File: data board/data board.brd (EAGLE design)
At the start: 31.6 x 28 mm, 28 parts, among them IC1 93LC56B, IC2 FT232HQ, X6 USBC, Y1 12MHz

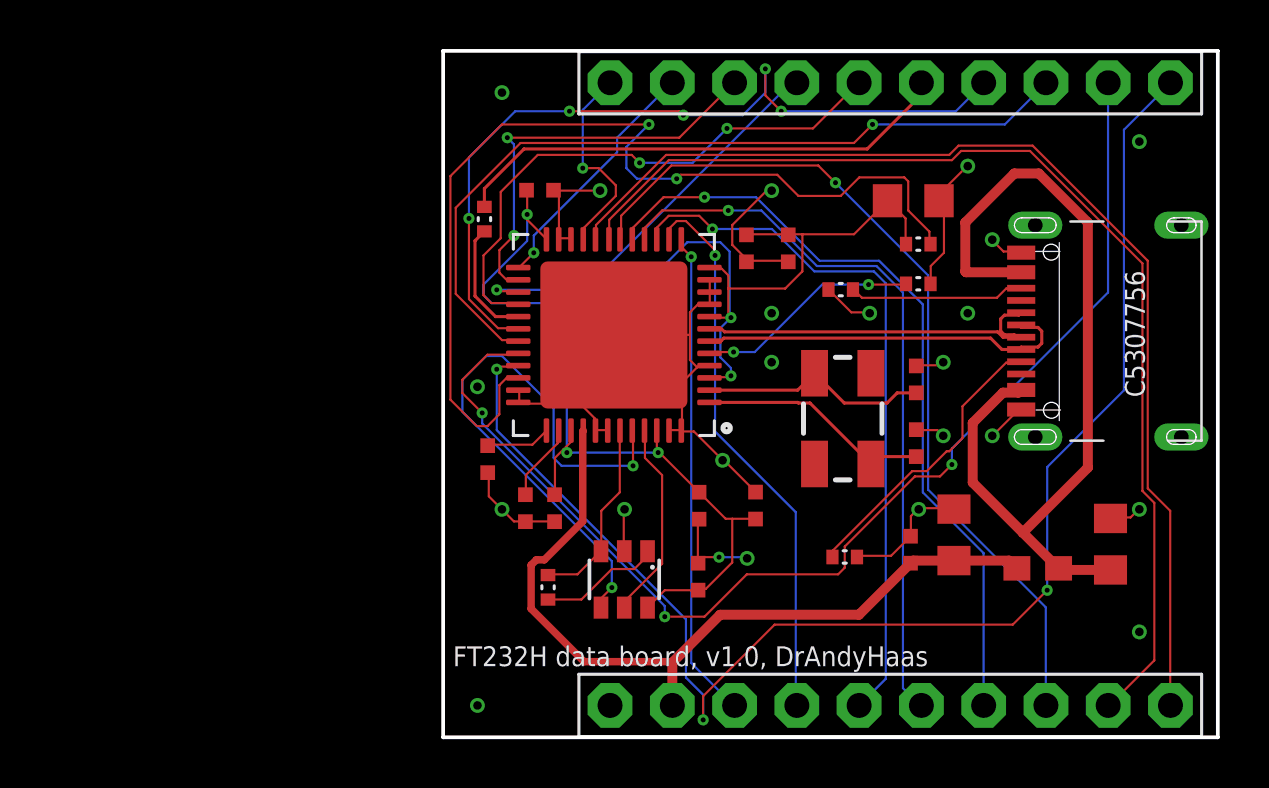
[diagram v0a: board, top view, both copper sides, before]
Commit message: add husb238 for power delivery
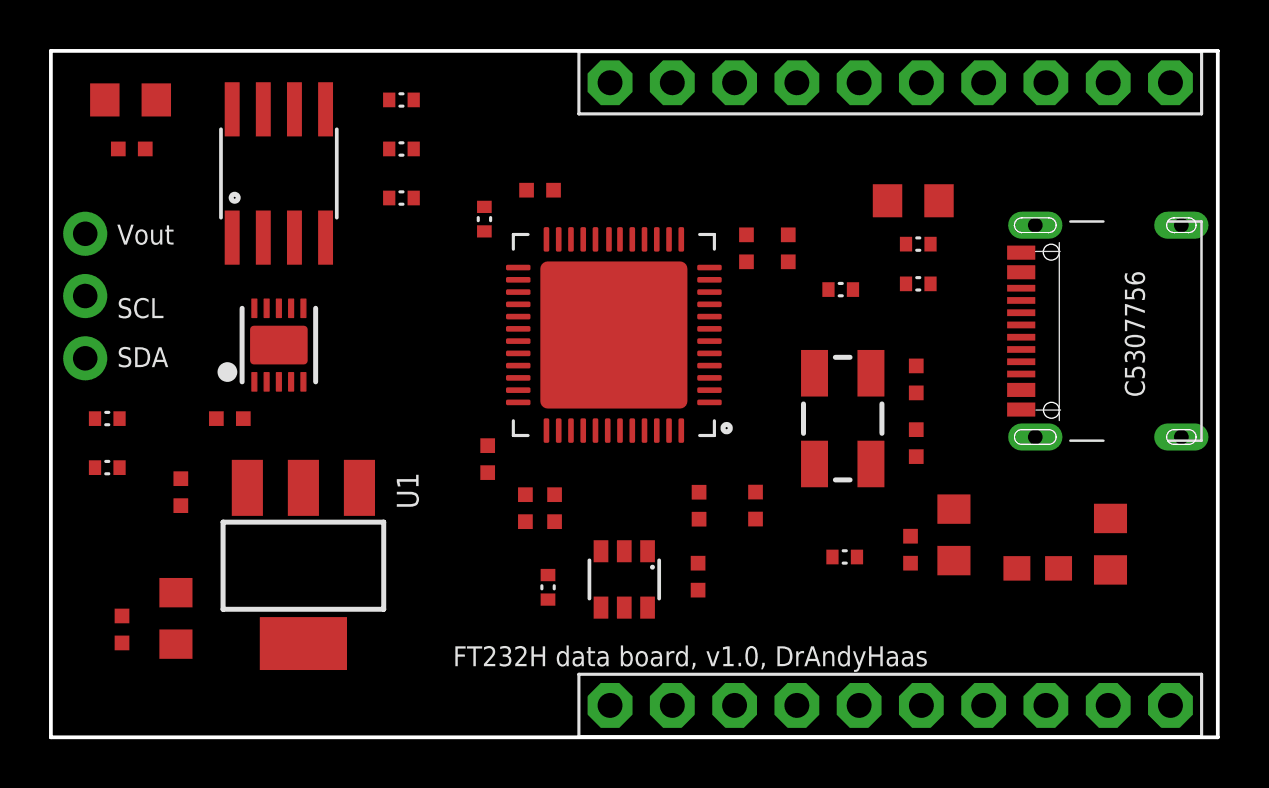
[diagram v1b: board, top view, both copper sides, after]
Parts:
- added C16: 1uF, Nordic_nRF:RESC0402_N
- added C17, C19: 10uF, Nordic_nRF:RESC0805_N
- added C18, C20, C21: 0.1uF, Nordic_nRF:RESC0402_N
- added JP3: (no value), microbuilder:1X03_ROUND
- added R10, R13: 10k, FlashPCB_Resistors:RES-0402
- added R7: 10, FlashPCB_Resistors:RES-0402
- added R8: 5.1k, FlashPCB_Resistors:RES-0402
- added R9: 49.9k, FlashPCB_Resistors:RES-0402
- added U$9: MOSFET-PCHANNEL-SOIC8SOIC8, SparkFun-DiscreteSemi:SO08
- added U1: CJT1117-5.0-SOT223, Seeed-IC:SOT-223
- added X3: HUSB238, adafruit_power:DFN10_3X3MM
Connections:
- new net GATE: R8.P$2, R9.P$1, U$9.4
- new net N$13: R13.P$1, X3.8
- new net N$14: R10.P$1, X3.9
- new net N$6: C16.2, R7.P$1, X3.1
- new net N$8: R8.P$1, X3.10
- new net SCL: JP3.2, X3.7
- new net SDA: JP3.3, X3.6
- new net VOUT: C17.2, C18.2, C21.2, JP3.1, U$9.5, U$9.6, U$9.7, U$9.8, U1.3
- net 5V: now also C19.2, C20.2, U1.2, U1.TER
- net CC1: now also X3.4
- net CC2: now also X3.5
- net D_N: now also X3.3
- net D_P: now also X3.2
- net GND: now also C16.1, C17.1, C18.1, C19.1, C20.1, C21.1, R10.P$2, R13.P$2, U1.1, X3.GND
- net VBUS: now also R7.P$2, R9.P$2, U$9.1, U$9.2, U$9.3
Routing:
- net VCC3V3: track 65.9 -> 0.00 mm, vias 5 -> 0
- net GND: track 63.8 -> 0.00 mm, vias 23 -> 0
- net C9: track 58.3 -> 0.00 mm, vias 3 -> 0
- net C8: track 48.8 -> 0.00 mm, vias 3 -> 0
- net D7: track 44.9 -> 0.00 mm
- net D6: track 44.7 -> 0.00 mm
- net N$7: track 40.4 -> 0.00 mm, vias 2 -> 0
- net VBUS: track 36.8 -> 0.00 mm
- net D5: track 35.7 -> 0.00 mm, vias 1 -> 0
- net C6: track 33.3 -> 0.00 mm, vias 5 -> 0
- net C7: track 33.1 -> 0.00 mm, vias 1 -> 0
- net 5V: track 32.6 -> 0.00 mm
- net D4: track 32.0 -> 0.00 mm, vias 1 -> 0
- net D3: track 29.9 -> 0.00 mm, vias 1 -> 0
- net D2: track 28.8 -> 0.00 mm, vias 1 -> 0
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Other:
- board size 31.6 x 28 mm -> 47.6 x 28 mm
- board text added: "SCL"
- board text added: "SDA"
- board text added: "Vout"

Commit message: Revert "add husb238 for power delivery"
This reverts commit fdcc09ca80390afb5c840c7f1bf23dbb25893304.
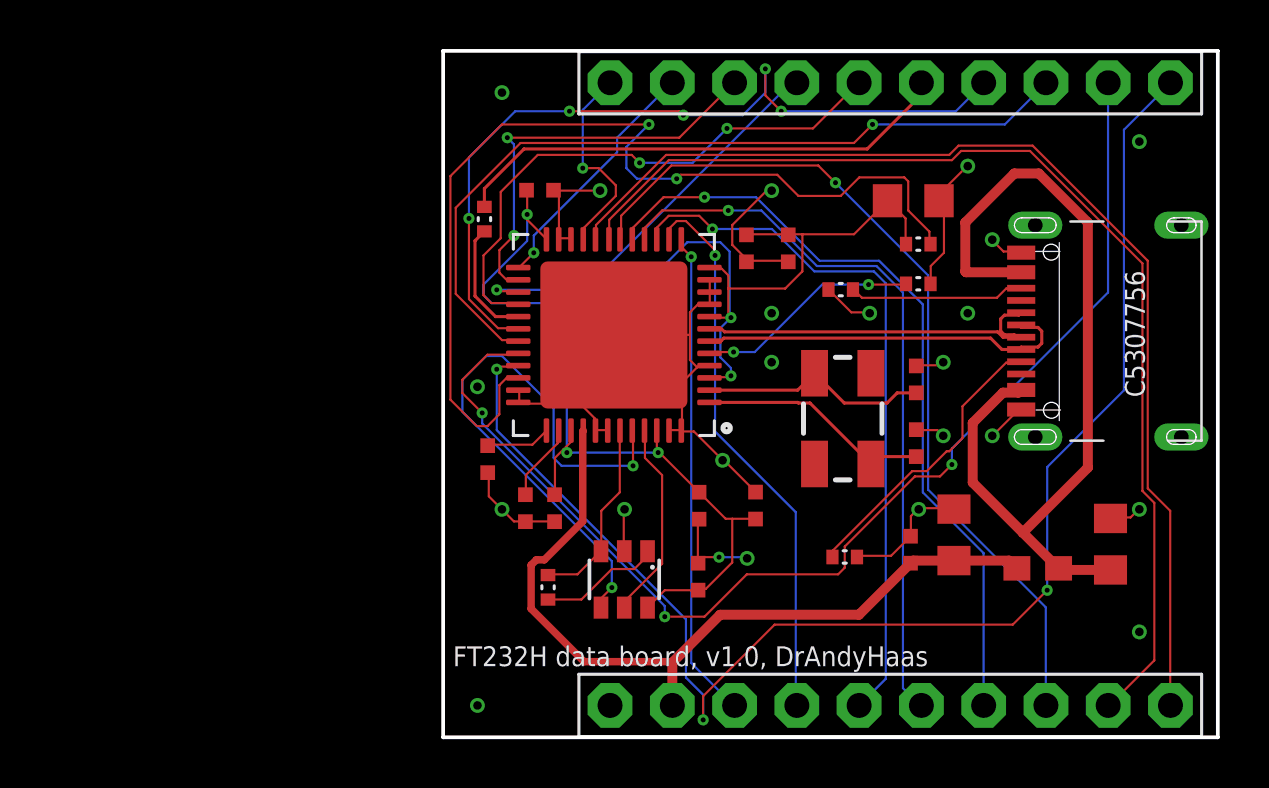
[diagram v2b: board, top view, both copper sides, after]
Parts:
- removed C16: 1uF, Nordic_nRF:RESC0402_N
- removed C17, C19: 10uF, Nordic_nRF:RESC0805_N
- removed C18, C20, C21: 0.1uF, Nordic_nRF:RESC0402_N
- removed JP3: (no value), microbuilder:1X03_ROUND
- removed R10, R13: 10k, FlashPCB_Resistors:RES-0402
- removed R7: 10, FlashPCB_Resistors:RES-0402
- removed R8: 5.1k, FlashPCB_Resistors:RES-0402
- removed R9: 49.9k, FlashPCB_Resistors:RES-0402
- removed U$9: MOSFET-PCHANNEL-SOIC8SOIC8, SparkFun-DiscreteSemi:SO08
- removed U1: CJT1117-5.0-SOT223, Seeed-IC:SOT-223
- removed X3: HUSB238, adafruit_power:DFN10_3X3MM
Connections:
- removed net GATE: R8.P$2, R9.P$1, U$9.4
- removed net N$13: R13.P$1, X3.8
- removed net N$14: R10.P$1, X3.9
- removed net N$6: C16.2, R7.P$1, X3.1
- removed net N$8: R8.P$1, X3.10
- removed net SCL: JP3.2, X3.7
- removed net SDA: JP3.3, X3.6
- removed net VOUT: C17.2, C18.2, C21.2, JP3.1, U$9.5, U$9.6, U$9.7, U$9.8, U1.3
- net 5V: no longer C19.2, C20.2, U1.2, U1.TER
- net CC1: no longer X3.4
- net CC2: no longer X3.5
- net D_N: no longer X3.3
- net D_P: no longer X3.2
- net GND: no longer C16.1, C17.1, C18.1, C19.1, C20.1, C21.1, R10.P$2, R13.P$2, U1.1, X3.GND
- net VBUS: no longer R7.P$2, R9.P$2, U$9.1, U$9.2, U$9.3
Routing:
- net VCC3V3: track 0.00 -> 65.9 mm, vias 0 -> 5
- net GND: track 0.00 -> 63.8 mm, vias 0 -> 23
- net C9: track 0.00 -> 58.3 mm, vias 0 -> 3
- net C8: track 0.00 -> 48.8 mm, vias 0 -> 3
- net D7: track 0.00 -> 44.9 mm
- net D6: track 0.00 -> 44.7 mm
- net N$7: track 0.00 -> 40.4 mm, vias 0 -> 2
- net VBUS: track 0.00 -> 36.8 mm
- net D5: track 0.00 -> 35.7 mm, vias 0 -> 1
- net C6: track 0.00 -> 33.3 mm, vias 0 -> 5
- net C7: track 0.00 -> 33.1 mm, vias 0 -> 1
- net 5V: track 0.00 -> 32.6 mm
- net D4: track 0.00 -> 32.0 mm, vias 0 -> 1
- net D3: track 0.00 -> 29.9 mm, vias 0 -> 1
- net D2: track 0.00 -> 28.8 mm, vias 0 -> 1
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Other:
- board size 47.6 x 28 mm -> 31.6 x 28 mm
- board text removed: "SCL"
- board text removed: "SDA"
- board text removed: "Vout"
